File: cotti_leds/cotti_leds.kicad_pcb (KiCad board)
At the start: 2 copper layers, 63.5 x 20.3 mm, 39 parts, among them J1 Pmod GPIO 1x06 pin, Q1 PMOS Kp=0.2A/V² |Vth|=0.8V, Q2 NMOS, Q3 PMOS Kp=0.2A/V² |Vth|=0.8V, Q4 NMOS, Q5 PMOS Kp=0.2A/V² |Vth|=0.8V, Q6 NMOS, Q7 PMOS Kp=0.2A/V² |Vth|=0.8V, Q8 NMOS, SW1 SW_4PDT

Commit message: feat: cotti_leds v0.0
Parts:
- removed the REF** at (130.5, 101.9)
- added REF**: cotti_logo_filled H=3mm T=0.3mm, Cotti_logo:cotti_logo_filled H=3mm T=0.3mm, F.Cu at (113.0, 113.2)
- moved JP4 25.7 mm to (133.3, 100.1), turned to 0 degrees
- moved JP3 20.6 mm to (129.5, 100.1), turned to 0 degrees
- moved R8 18.3 mm to (140.0, 115.3)
- moved R7 17.6 mm to (140.0, 110.5)
- moved R6 17.1 mm to (140.0, 105.7)
- moved R5 17.0 mm to (140.0, 100.8)
- moved JP2 15.5 mm to (125.7, 100.1), turned to 0 degrees
- moved JP1 10.9 mm to (121.9, 100.1), turned to 0 degrees
- moved J1 8.03 mm to (110.5, 100.3)
- moved R1 7.33 mm to (113.8, 104.6)
- moved R2 7.22 mm to (113.8, 106.7)
- moved R3 7.15 mm to (113.8, 108.7)
- moved R4 7.12 mm to (113.8, 110.7)
- moved D4 4.88 mm to (154.9, 114.3), turned to 90 degrees
- moved D3 4.72 mm to (154.9, 109.5), turned to 90 degrees
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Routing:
- net /vcc3: track 57.2 -> 34.5 mm, vias 3 -> 2
- net /vcc4: track 46.8 -> 28.9 mm, vias 3 -> 2
- net /io4: track 7.04 -> 22.5 mm
- net /vcc2: track 44.0 -> 29.4 mm, vias 3 -> 2
- net /io4_L: track 37.0 -> 23.2 mm
- net /io4_H: track 37.4 -> 24.2 mm
- net /io3_L: track 37.7 -> 24.9 mm
- net VCC: track 38.1 -> 25.7 mm
- net Net-(R6-Pad1): track 21.5 -> 10.2 mm, vias 2 -> 0
- net Net-(R8-Pad1): track 20.3 -> 9.08 mm, vias 2 -> 0
- net /io3: track 6.51 -> 17.7 mm
- net /io3_H: track 36.4 -> 25.9 mm
- net /io2_H: track 35.5 -> 26.7 mm
- net /io1_H: track 36.2 -> 28.0 mm
- net /io2_L: track 35.9 -> 27.9 mm
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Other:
- board size 63.5 x 20.3 mm -> 50.8 x 20.3 mm

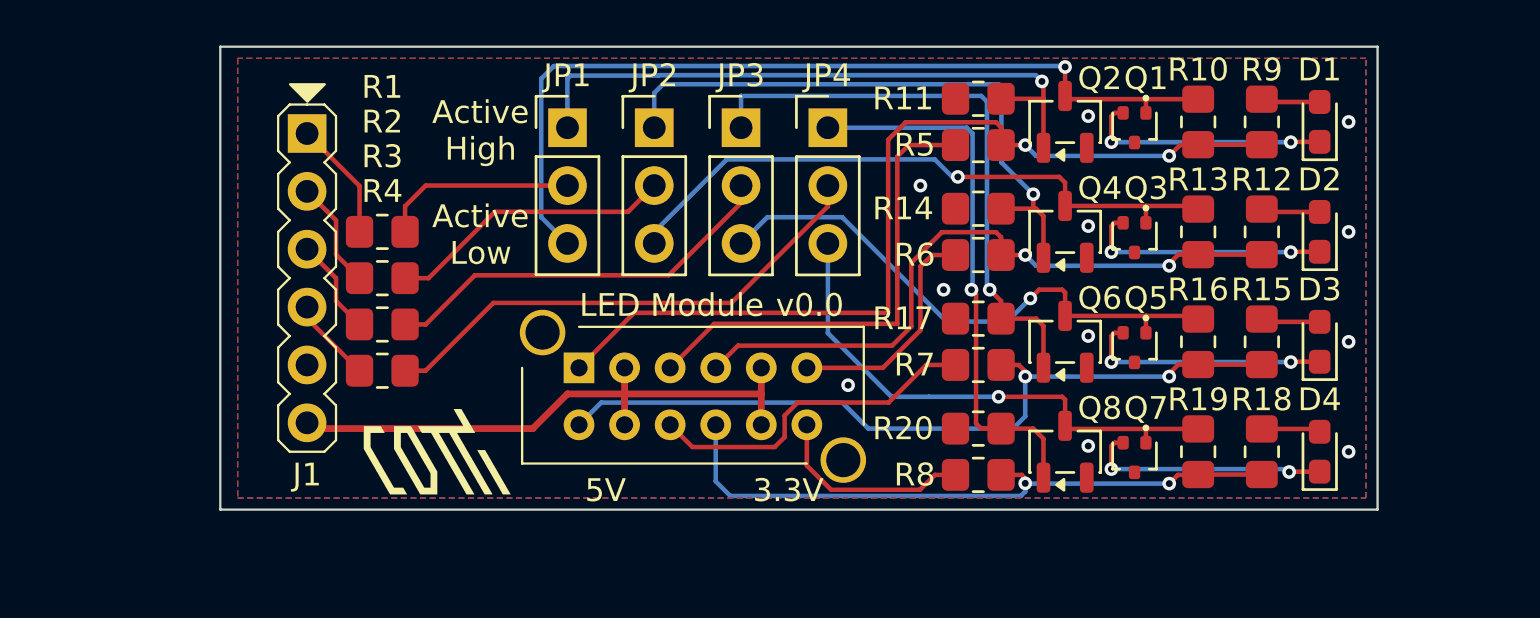
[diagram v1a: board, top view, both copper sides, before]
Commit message: feat: cotti leds with new library format
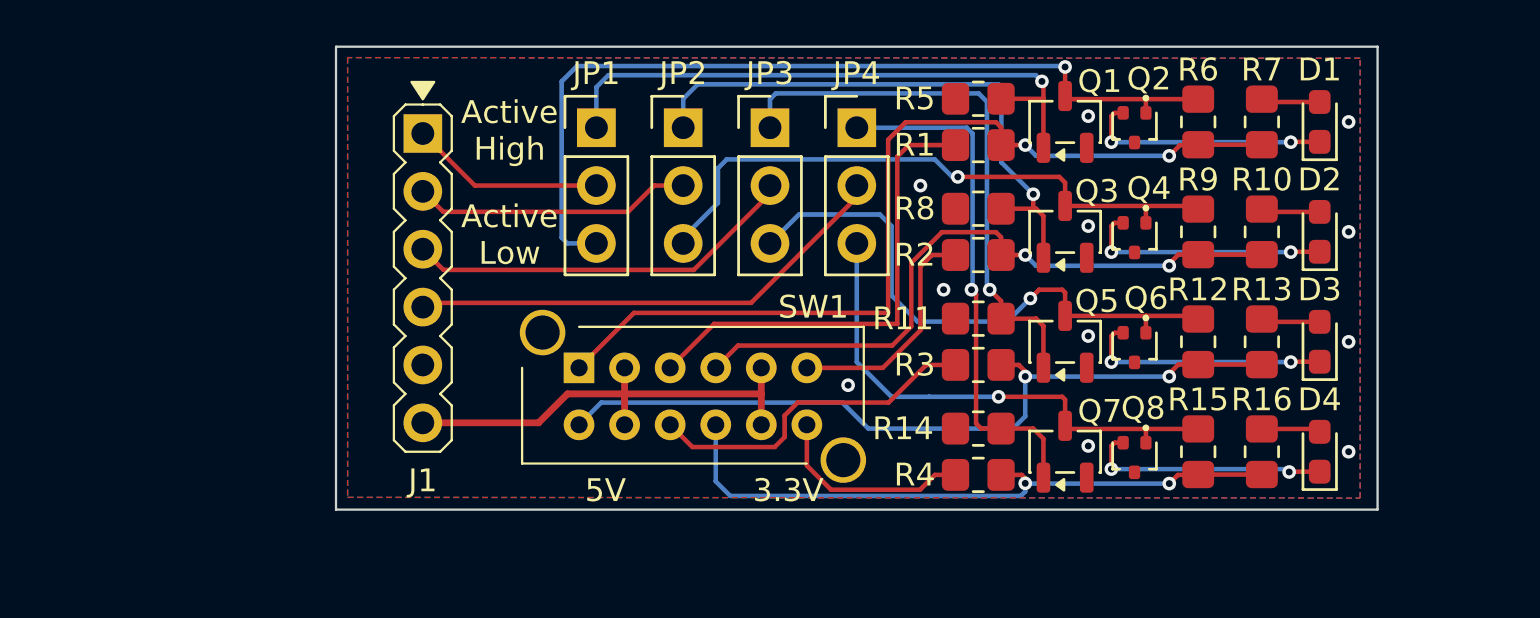
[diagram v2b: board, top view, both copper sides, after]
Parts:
- removed the R1 at (113.8, 104.6)
- removed the R2 at (113.8, 106.7)
- removed the R3 at (113.8, 108.7)
- removed the R4 at (113.8, 110.7)
- removed the REF** at (113.0, 113.2)
- added REF**: cotti_logo_filled H=7.5mm T=0.75mm, cotti_logo:cotti_logo_filled H=7.5mm T=0.75mm, B.Cu at (154.6, 107.0)
- D1, D2, D3, D4: value Green Vf=2V If=0-20mA -> Red Vf=2V If=10mA
- J1: footprint Pmod:Pmod_1x06_pin -> cotti_footprints:Pmod_1x06_pin
- JP1: value IO1 L/H -> IO1
- JP2: value IO2 L/H -> IO2
- JP3: value IO3 L/H -> IO3
- JP4: value IO4 L/H -> IO4
- Q1, Q3, Q5, Q7: value PMOS Kp=0.2A/V² |Vth|=0.8V -> 2N7002K; footprint footprints:local_SOT-416 -> Package_TO_SOT_SMD:SOT-23-3
- Q2, Q4, Q6, Q8: value NMOS -> RE1C001ZPTL; footprint Package_TO_SOT_SMD:SOT-23-3 -> Package_TO_SOT_SMD:SOT-416
- SW1: footprint Cotti_misc:SW_4PDT -> cotti_footprints:SW_4PDT
- moved J1 5.08 mm to (115.6, 100.3)
- moved Q3 3.06 mm to (143.8, 104.6), turned to 90 degrees
- moved Q4 3.06 mm to (146.8, 104.9), turned to -90 degrees
- moved Q7 3.06 mm to (143.8, 114.3), turned to 90 degrees
- moved Q8 3.06 mm to (146.8, 114.6), turned to -90 degrees
- moved Q1 3.06 mm to (143.8, 99.8), turned to 90 degrees
- moved Q2 3.06 mm to (146.8, 100.1), turned to -90 degrees
- moved Q5 3.06 mm to (143.8, 109.5), turned to 90 degrees
- moved Q6 3.06 mm to (146.8, 109.7), turned to -90 degrees
- moved JP3 1.27 mm to (130.8, 100.1)
- moved JP4 1.27 mm to (134.6, 100.1)
- moved JP1 1.27 mm to (123.2, 100.1)
- moved JP2 1.27 mm to (127.0, 100.1)
- renumbered R5 to R1, R12 to R10, R17 to R11, R16 to R12, R15 to R13, R20 to R14, R19 to R15, R18 to R16, R6 to R2, R7 to R3, R8 to R4, R11 to R5, R10 to R6, R9 to R7, R14 to R8, R13 to R9
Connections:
- J1 pad 1: Net-(J1-IO1) -> /io1
- J1 pad 2: Net-(J1-IO2/PWM) -> /io2
- J1 pad 3: Net-(J1-IO3) -> /io3
- J1 pad 4: Net-(J1-IO4) -> /io4
- Q1 pad 1: /io1_L -> /io1_H
- Q1 pad 2: Net-(D1-K) -> GND
- Q1 pad 3: GND -> /io1_L
- Q2 pad 1: /io1_H -> /io1_L
- Q2 pad 2: GND -> Net-(D1-K)
- Q2 pad 3: /io1_L -> GND
- Q3 pad 1: /io2_L -> /io2_H
- Q3 pad 2: Net-(D2-K) -> GND
- Q3 pad 3: GND -> /io2_L
- Q4 pad 1: /io2_H -> /io2_L
- Q4 pad 2: GND -> Net-(D2-K)
- Q4 pad 3: /io2_L -> GND
- Q5 pad 1: /io3_L -> /io3_H
- Q5 pad 2: Net-(D3-K) -> GND
- Q5 pad 3: GND -> /io3_L
- Q6 pad 1: /io3_H -> /io3_L
- Q6 pad 2: GND -> Net-(D3-K)
- Q6 pad 3: /io3_L -> GND
- Q7 pad 1: /io4_L -> /io4_H
- Q7 pad 2: Net-(D4-K) -> GND
- Q7 pad 3: GND -> /io4_L
- Q8 pad 1: /io4_H -> /io4_L
- Q8 pad 2: GND -> Net-(D4-K)
- Q8 pad 3: /io4_L -> GND
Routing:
- net VCC: track 25.7 -> 20.4 mm
- net Net-(J1-IO1): track 5.27 -> 0.00 mm
- net Net-(J1-IO2/PWM): track 4.76 -> 0.00 mm
- net Net-(J1-IO3): track 4.26 -> 0.00 mm
- net Net-(J1-IO4): track 3.75 -> 0.00 mm
- net /io1_H: track 28.0 -> 26.5 mm
- net /io2_H: track 26.7 -> 25.3 mm
- net /io4_H: track 24.2 -> 23.0 mm
- net /io3_H: track 25.9 -> 24.6 mm
- net /io4: track 22.5 -> 21.6 mm
- net /io1: track 8.63 -> 9.29 mm
- net /io3_L: track 24.9 -> 25.5 mm
- net /io4_L: track 23.2 -> 22.7 mm
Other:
- board size 50.8 x 20.3 mm -> 45.7 x 20.3 mm
- board text added: "Rev 0.0"
- board text removed: "v0.0"

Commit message: feat: cotti leds gerber files
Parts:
- Q2, Q4, Q6, Q8: footprint Package_TO_SOT_SMD:SOT-416 -> cotti_footprints:SOT-416
- moved J1 2.54 mm to (113.0, 100.3)
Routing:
- net /io4: track 21.6 -> 24.1 mm
- net /io3: track 17.4 -> 19.9 mm
- net VCC: track 20.4 -> 22.9 mm
- net /io2: track 12.3 -> 14.8 mm
- net /io1: track 9.29 -> 11.8 mm
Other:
- board size 45.7 x 20.3 mm -> 48.3 x 20.3 mm
- board text added: "D1"
- board text added: "D2"
- board text added: "D3"
- board text added: "D4"
- board text added: "GND"
- board text added: "VCC"
